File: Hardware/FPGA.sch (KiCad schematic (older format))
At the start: 25 parts, among them U501 W25Q128JVxxM, U502 ICE40UP5K-SG48, U503 Crystal Oscillator, U504 USBLC6-2

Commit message: Nothing to see here.
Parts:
- gave numbers to parts that had none: 9
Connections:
- net AMP_VOL: now also U502.4 (IOB_8A)
- net TRRS_Ring1_Switch: now reaches U502.2 (IOB_6A)
- net TRRS_Tip_Switch: now reaches U502.3 (IOB_9B)
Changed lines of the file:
@@
 $Descr A4 11693 8268
 encoding utf-8
-Sheet 5 7
+Sheet 2 7
 Title ""
 Date ""
@@
 	8000 1850 7450 1850
 Text HLabel 5350 1950 0    50   Input ~ 0
-TRRS_Ring2_Switch
+TRRS_Ring1_Switch
 Text HLabel 5350 2150 0    50   Input ~ 0
-TRRS_Sleeve_Switch
+TRRS_Tip_Switch
 Text Label 7550 3650 0    50   ~ 0
 i2c0_SDA
@@
 P 9000 900
 AR Path="/612429E8/616CDFC9" Ref="TP?"  Part="1"
-AR Path="/611E3335/616CDFC9" Ref="TP?"  Part="1"
-F 0 "TP?" H 9058 1018 50  0000 L CNN
+AR Path="/611E3335/616CDFC9" Ref="TP501"  Part="1"
+F 0 "TP501" H 9058 1018 50  0000 L CNN
 F 1 "1v2" H 9058 927 50  0000 L CNN
 F 2 "TestPoint:TestPoint_THTPad_D1.5mm_Drill0.7mm" H 9200 900 50  0001 C CNN
@@
 P 9600 900
 AR Path="/612429E8/616D59B5" Ref="TP?"  Part="1"
-AR Path="/611E3335/616D59B5" Ref="TP?"  Part="1"
-F 0 "TP?" H 9658 1018 50  0000 L CNN
+AR Path="/611E3335/616D59B5" Ref="TP502"  Part="1"
+F 0 "TP502" H 9658 1018 50  0000 L CNN
 F 1 "2v5" H 9658 927 50  0000 L CNN
 F 2 "TestPoint:TestPoint_THTPad_D1.5mm_Drill0.7mm" H 9800 900 50  0001 C CNN
@@
 P 10300 900
 AR Path="/612429E8/616D5D99" Ref="TP?"  Part="1"
-AR Path="/611E3335/616D5D99" Ref="TP?"  Part="1"
-F 0 "TP?" H 10358 1018 50  0000 L CNN
+AR Path="/611E3335/616D5D99" Ref="TP503"  Part="1"
+F 0 "TP503" H 10358 1018 50  0000 L CNN
 F 1 "3v3" H 10358 927 50  0000 L CNN
 F 2 "TestPoint:TestPoint_THTPad_D1.5mm_Drill0.7mm" H 10500 900 50  0001 C CNN
@@
 AR Path="/612429E8/617082A2" Ref="Sp?"  Part="1"
 AR Path="/617082A2" Ref="Sp?"  Part="1"
-AR Path="/611E3335/617082A2" Ref="Sp?"  Part="1"
-F 0 "Sp?" H 9150 5750 50  0000 R CNN
+AR Path="/611E3335/617082A2" Ref="Sp501"  Part="1"
+F 0 "Sp501" H 9150 5750 50  0000 R CNN
 F 1 "49a" H 9150 5650 50  0000 R CNN
 F 2 "TestPoint:TestPoint_THTPad_D2.5mm_Drill1.2mm" H 9400 5600 50  0001 C CNN
@@
 AR Path="/612429E8/6171C233" Ref="Sp?"  Part="1"
 AR Path="/6171C233" Ref="Sp?"  Part="1"
-AR Path="/611E3335/6171C233" Ref="Sp?"  Part="1"
-F 0 "Sp?" H 9750 5750 50  0000 R CNN
+AR Path="/611E3335/6171C233" Ref="Sp503"  Part="1"
+F 0 "Sp503" H 9750 5750 50  0000 R CNN
 F 1 "50b" H 9750 5650 50  0000 R CNN
 F 2 "TestPoint:TestPoint_THTPad_D2.5mm_Drill1.2mm" H 10000 5600 50  0001 C CNN
@@
 AR Path="/612429E8/6171C94C" Ref="Sp?"  Part="1"
 AR Path="/6171C94C" Ref="Sp?"  Part="1"
-AR Path="/611E3335/6171C94C" Ref="Sp?"  Part="1"
-F 0 "Sp?" H 10250 5750 50  0000 R CNN
+AR Path="/611E3335/6171C94C" Ref="Sp505"  Part="1"
+F 0 "Sp505" H 10250 5750 50  0000 R CNN
 F 1 "51a" H 10250 5650 50  0000 R CNN
 F 2 "TestPoint:TestPoint_THTPad_D2.5mm_Drill1.2mm" H 10500 5600 50  0001 C CNN
@@
 AR Path="/612429E8/617269B8" Ref="Sp?"  Part="1"
 AR Path="/617269B8" Ref="Sp?"  Part="1"
-AR Path="/611E3335/617269B8" Ref="Sp?"  Part="1"
-F 0 "Sp?" H 9150 6150 50  0000 R CNN
+AR Path="/611E3335/617269B8" Ref="Sp502"  Part="1"
+F 0 "Sp502" H 9150 6150 50  0000 R CNN
 F 1 "20a" H 9150 6050 50  0000 R CNN
 F 2 "TestPoint:TestPoint_THTPad_D2.5mm_Drill1.2mm" H 9400 6000 50  0001 C CNN
@@
 AR Path="/612429E8/617269BE" Ref="Sp?"  Part="1"
 AR Path="/617269BE" Ref="Sp?"  Part="1"
-AR Path="/611E3335/617269BE" Ref="Sp?"  Part="1"
-F 0 "Sp?" H 9750 6150 50  0000 R CNN
+AR Path="/611E3335/617269BE" Ref="Sp504"  Part="1"
+F 0 "Sp504" H 9750 6150 50  0000 R CNN
 F 1 "22a" H 9750 6050 50  0000 R CNN
 F 2 "TestPoint:TestPoint_THTPad_D2.5mm_Drill1.2mm" H 10000 6000 50  0001 C CNN
@@
 AR Path="/612429E8/617269C6" Ref="Sp?"  Part="1"
 AR Path="/617269C6" Ref="Sp?"  Part="1"
-AR Path="/611E3335/617269C6" Ref="Sp?"  Part="1"
-F 0 "Sp?" H 10250 6150 50  0000 R CNN
+AR Path="/611E3335/617269C6" Ref="Sp506"  Part="1"
+F 0 "Sp506" H 10250 6150 50  0000 R CNN
 F 1 "25b_g3" H 10250 6050 50  0000 R CNN
 F 2 "TestPoint:TestPoint_THTPad_D2.5mm_Drill1.2mm" H 10500 6000 50  0001 C CNN
@@
 Wire Wire Line
 	10300 6100 10300 6000
+Wire Wire Line
+	5350 1950 5450 1950
+Wire Wire Line
+	5350 2050 5450 2050
+Wire Wire Line
+	5350 2150 5450 2150
 $EndSCHEMATC

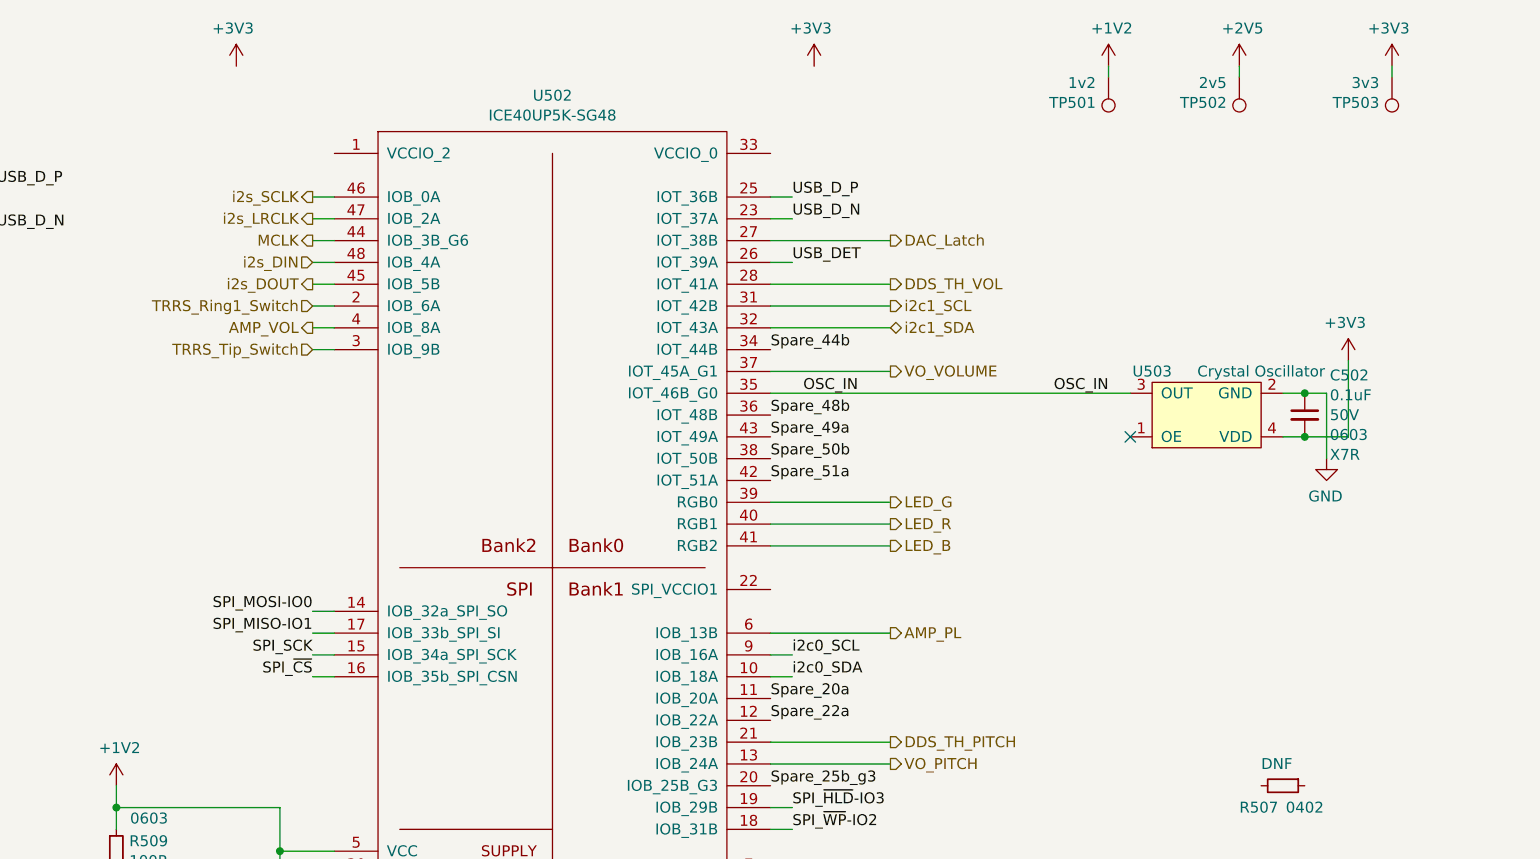
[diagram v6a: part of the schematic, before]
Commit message: Adding in extra decoupling.
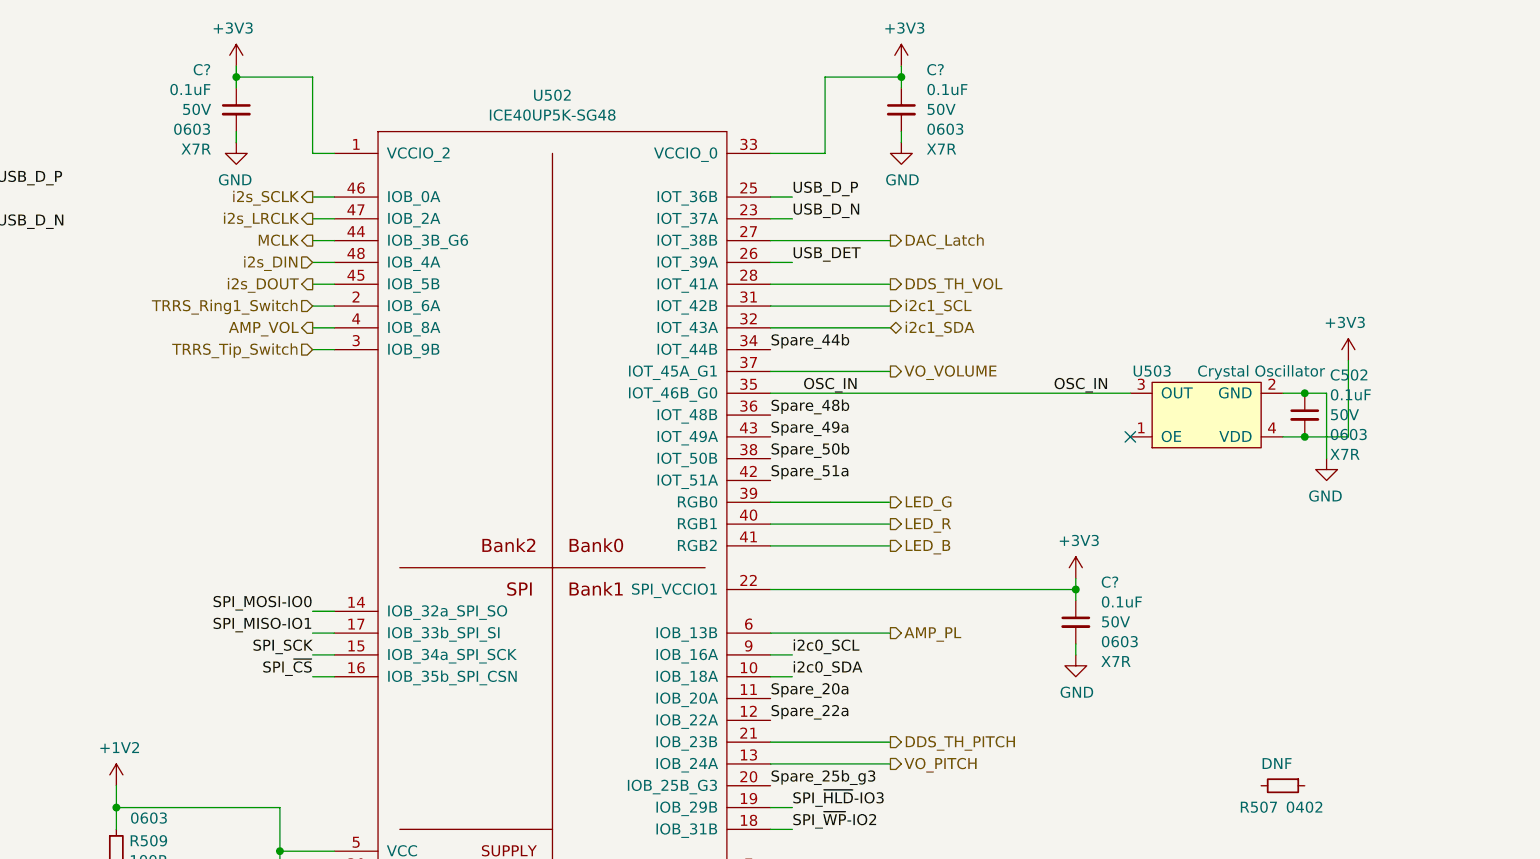
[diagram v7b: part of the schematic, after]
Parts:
- removed TP501: 1v2, TestPoint:TestPoint_THTPad_D1.5mm_Drill0.7mm, symbol Connector:TestPoint
- removed TP502: 2v5, TestPoint:TestPoint_THTPad_D1.5mm_Drill0.7mm, symbol Connector:TestPoint
- removed TP503: 3v3, TestPoint:TestPoint_THTPad_D1.5mm_Drill0.7mm, symbol Connector:TestPoint
- added C? (x3): 0.1uF, Capacitor_SMD:C_0603_1608Metric, symbol Device:C_Small
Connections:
- net +3V3: now also U502.1 (VCCIO_2), U502.22 (SPI_VCCIO1), U502.33 (VCCIO_0), C?.1, C?.1, C?.1
- net GND: now also C?.2, C?.2, C?.2
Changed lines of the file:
@@
 	5000 4950 5000 4900
-$Comp
-L power:+1V2 #PWR?
-U 1 1 6174C4EC
-P 9000 850
-AR Path="/6123BB15/6174C4EC" Ref="#PWR?"  Part="1"
-AR Path="/611E335F/6174C4EC" Ref="#PWR?"  Part="1"
-AR Path="/611E3335/6174C4EC" Ref="#PWR0166"  Part="1"
-F 0 "#PWR0166" H 9000 700 50  0001 C CNN
-F 1 "+1V2" H 9015 1023 50  0000 C CNN
-F 2 "" H 9000 850 50  0001 C CNN
-F 3 "" H 9000 850 50  0001 C CNN
-	1    9000 850
-	1    0    0    -1
-$EndComp
-$Comp
-L power:+2V5 #PWR?
-U 1 1 6174CE7E
-P 9600 850
-AR Path="/6123BB15/6174CE7E" Ref="#PWR?"  Part="1"
-AR Path="/611E335F/6174CE7E" Ref="#PWR?"  Part="1"
-AR Path="/611E3335/6174CE7E" Ref="#PWR0167"  Part="1"
-F 0 "#PWR0167" H 9600 700 50  0001 C CNN
-F 1 "+2V5" H 9615 1023 50  0000 C CNN
-F 2 "" H 9600 850 50  0001 C CNN
-F 3 "" H 9600 850 50  0001 C CNN
-	1    9600 850
-	1    0    0    -1
-$EndComp
-$Comp
-L power:+3V3 #PWR0168
-U 1 1 6174EEF9
-P 10300 850
-F 0 "#PWR0168" H 10300 700 50  0001 C CNN
-F 1 "+3V3" H 10315 1023 50  0000 C CNN
-F 2 "" H 10300 850 50  0001 C CNN
-F 3 "" H 10300 850 50  0001 C CNN
-	1    10300 850
-	-1   0    0    -1
-$EndComp
 $Comp
 L power:+3V3 #PWR0169
@@
 Wire Wire Line
 	7450 1450 7550 1450
-$Comp
-L power:+3V3 #PWR0170
-U 1 1 61762CA8
-P 7650 850
-F 0 "#PWR0170" H 7650 700 50  0001 C CNN
-F 1 "+3V3" H 7665 1023 50  0000 C CNN
-F 2 "" H 7650 850 50  0001 C CNN
-F 3 "" H 7650 850 50  0001 C CNN
-	1    7650 850
-	-1   0    0    -1
-$EndComp
 Text Label 7550 1750 0    50   ~ 0
 USB_DET
@@
 Wire Wire Line
 	1300 4700 1400 4700
-$Comp
-L Connector:TestPoint TP?
-U 1 1 616CDFC9
-P 9000 900
-AR Path="/612429E8/616CDFC9" Ref="TP?"  Part="1"
-AR Path="/611E3335/616CDFC9" Ref="TP501"  Part="1"
-F 0 "TP501" H 9058 1018 50  0000 L CNN
-F 1 "1v2" H 9058 927 50  0000 L CNN
-F 2 "TestPoint:TestPoint_THTPad_D1.5mm_Drill0.7mm" H 9200 900 50  0001 C CNN
-F 3 "~" H 9200 900 50  0001 C CNN
-	1    9000 900
-	-1   0    0    1
-$EndComp
-Wire Wire Line
-	9000 900  9000 850
-$Comp
-L Connector:TestPoint TP?
-U 1 1 616D59B5
-P 9600 900
-AR Path="/612429E8/616D59B5" Ref="TP?"  Part="1"
-AR Path="/611E3335/616D59B5" Ref="TP502"  Part="1"
-F 0 "TP502" H 9658 1018 50  0000 L CNN
-F 1 "2v5" H 9658 927 50  0000 L CNN
-F 2 "TestPoint:TestPoint_THTPad_D1.5mm_Drill0.7mm" H 9800 900 50  0001 C CNN
-F 3 "~" H 9800 900 50  0001 C CNN
-	1    9600 900
-	-1   0    0    1
-$EndComp
-$Comp
-L Connector:TestPoint TP?
-U 1 1 616D5D99
-P 10300 900
-AR Path="/612429E8/616D5D99" Ref="TP?"  Part="1"
-AR Path="/611E3335/616D5D99" Ref="TP503"  Part="1"
-F 0 "TP503" H 10358 1018 50  0000 L CNN
-F 1 "3v3" H 10358 927 50  0000 L CNN
-F 2 "TestPoint:TestPoint_THTPad_D1.5mm_Drill0.7mm" H 10500 900 50  0001 C CNN
-F 3 "~" H 10500 900 50  0001 C CNN
-	1    10300 900
-	-1   0    0    1
-$EndComp
-Wire Wire Line
-	9600 900  9600 850
-Wire Wire Line
-	10300 900  10300 850
 $Comp
 L OpenThereminCC-rescue:TEST_1P GROUND?
@@
 Wire Wire Line
 	5350 2150 5450 2150
+$Comp
+L Device:C_Small C?
+U 1 1 61497B20
+P 5000 1050
+AR Path="/611E335F/61497B20" Ref="C?"  Part="1"
+AR Path="/611E3335/61497B20" Ref="C?"  Part="1"
+F 0 "C?" H 5115 1232 50  0000 L CNN
+F 1 "0.1uF" H 5115 1141 50  0000 L CNN
+F 2 "Capacitor_SMD:C_0603_1608Metric" H 5038 900 50  0001 C CNN
+F 3 "~" H 5000 1050 50  0001 C CNN
+F 4 "C0603C104K5RACAUTO" H 5000 1050 50  0001 C CNN "MPN"
+F 5 "399-6856-1-ND" H 5000 1050 50  0001 C CNN "DPN"
+F 6 "50V" H 5115 1050 50  0000 L CNN "Tol"
+F 7 "0603" H 5115 959 50  0000 L CNN "Pkg"
+F 8 "X7R" H 5115 868 50  0000 L CNN "TCoff"
+	1    5000 1050
+	-1   0    0    -1
+$EndComp
+$Comp
+L power:GND #PWR?
+U 1 1 6149AB04
+P 5000 1200
+F 0 "#PWR?" H 5000 950 50  0001 C CNN
+F 1 "GND" H 5005 1027 50  0000 C CNN
+F 2 "" H 5000 1200 50  0001 C CNN
+F 3 "" H 5000 1200 50  0001 C CNN
+	1    5000 1200
+	-1   0    0    -1
+$EndComp
+Wire Wire Line
+	5000 850  5000 900
+Wire Wire Line
+	5000 1150 5000 1200
+Wire Wire Line
+	5000 900  5350 900
+Wire Wire Line
+	5350 900  5350 1250
+Wire Wire Line
+	5350 1250 5450 1250
+Connection ~ 5000 900
+Wire Wire Line
+	5000 900  5000 950
+$Comp
+L power:+3V3 #PWR?
+U 1 1 614A844D
+P 8050 850
+F 0 "#PWR?" H 8050 700 50  0001 C CNN
+F 1 "+3V3" H 8065 1023 50  0000 C CNN
+F 2 "" H 8050 850 50  0001 C CNN
+F 3 "" H 8050 850 50  0001 C CNN
+	1    8050 850
+	1    0    0    -1
+$EndComp
+$Comp
+L Device:C_Small C?
+U 1 1 614A8458
+P 8050 1050
+AR Path="/611E335F/614A8458" Ref="C?"  Part="1"
+AR Path="/611E3335/614A8458" Ref="C?"  Part="1"
+F 0 "C?" H 8165 1232 50  0000 L CNN
+F 1 "0.1uF" H 8165 1141 50  0000 L CNN
+F 2 "Capacitor_SMD:C_0603_1608Metric" H 8088 900 50  0001 C CNN
+F 3 "~" H 8050 1050 50  0001 C CNN
+F 4 "C0603C104K5RACAUTO" H 8050 1050 50  0001 C CNN "MPN"
+F 5 "399-6856-1-ND" H 8050 1050 50  0001 C CNN "DPN"
+F 6 "50V" H 8165 1050 50  0000 L CNN "Tol"
+F 7 "0603" H 8165 959 50  0000 L CNN "Pkg"
+F 8 "X7R" H 8165 868 50  0000 L CNN "TCoff"
+	1    8050 1050
+	1    0    0    -1
+$EndComp
+$Comp
+L power:GND #PWR?
+U 1 1 614A845E
+P 8050 1200
+F 0 "#PWR?" H 8050 950 50  0001 C CNN
+F 1 "GND" H 8055 1027 50  0000 C CNN
+F 2 "" H 8050 1200 50  0001 C CNN
+F 3 "" H 8050 1200 50  0001 C CNN
+	1    8050 1200
+	1    0    0    -1
+$EndComp
+Wire Wire Line
+	8050 850  8050 900
+Wire Wire Line
+	8050 1150 8050 1200
+Wire Wire Line
+	8050 900  7700 900
+Connection ~ 8050 900
+Wire Wire Line
+	8050 900  8050 950
+Wire Wire Line
+	7700 900  7700 1250
+Wire Wire Line
+	7700 1250 7450 1250
+$Comp
+L power:+3V3 #PWR?
+U 1 1 614B4975
+P 8850 3200
+F 0 "#PWR?" H 8850 3050 50  0001 C CNN
+F 1 "+3V3" H 8865 3373 50  0000 C CNN
+F 2 "" H 8850 3200 50  0001 C CNN
+F 3 "" H 8850 3200 50  0001 C CNN
+	1    8850 3200
+	1    0    0    -1
+$EndComp
+$Comp
+L Device:C_Small C?
+U 1 1 614B4980
+P 8850 3400
+AR Path="/611E335F/614B4980" Ref="C?"  Part="1"
+AR Path="/611E3335/614B4980" Ref="C?"  Part="1"
+F 0 "C?" H 8965 3582 50  0000 L CNN
+F 1 "0.1uF" H 8965 3491 50  0000 L CNN
+F 2 "Capacitor_SMD:C_0603_1608Metric" H 8888 3250 50  0001 C CNN
+F 3 "~" H 8850 3400 50  0001 C CNN
+F 4 "C0603C104K5RACAUTO" H 8850 3400 50  0001 C CNN "MPN"
+F 5 "399-6856-1-ND" H 8850 3400 50  0001 C CNN "DPN"
+F 6 "50V" H 8965 3400 50  0000 L CNN "Tol"
+F 7 "0603" H 8965 3309 50  0000 L CNN "Pkg"
+F 8 "X7R" H 8965 3218 50  0000 L CNN "TCoff"
+	1    8850 3400
+	1    0    0    -1
+$EndComp
+$Comp
+L power:GND #PWR?
+U 1 1 614B4986
+P 8850 3550
+F 0 "#PWR?" H 8850 3300 50  0001 C CNN
+F 1 "GND" H 8855 3377 50  0000 C CNN
+F 2 "" H 8850 3550 50  0001 C CNN
+F 3 "" H 8850 3550 50  0001 C CNN
+	1    8850 3550
+	1    0    0    -1
+$EndComp
+Wire Wire Line
+	8850 3200 8850 3250
+Wire Wire Line
+	8850 3500 8850 3550
+Connection ~ 8850 3250
+Wire Wire Line
+	8850 3250 8850 3300
+Wire Wire Line
+	7450 3250 8850 3250
 $EndSCHEMATC
